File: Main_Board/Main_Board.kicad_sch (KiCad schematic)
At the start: 3 parts, among them U1 TCR2EF33_LMCT

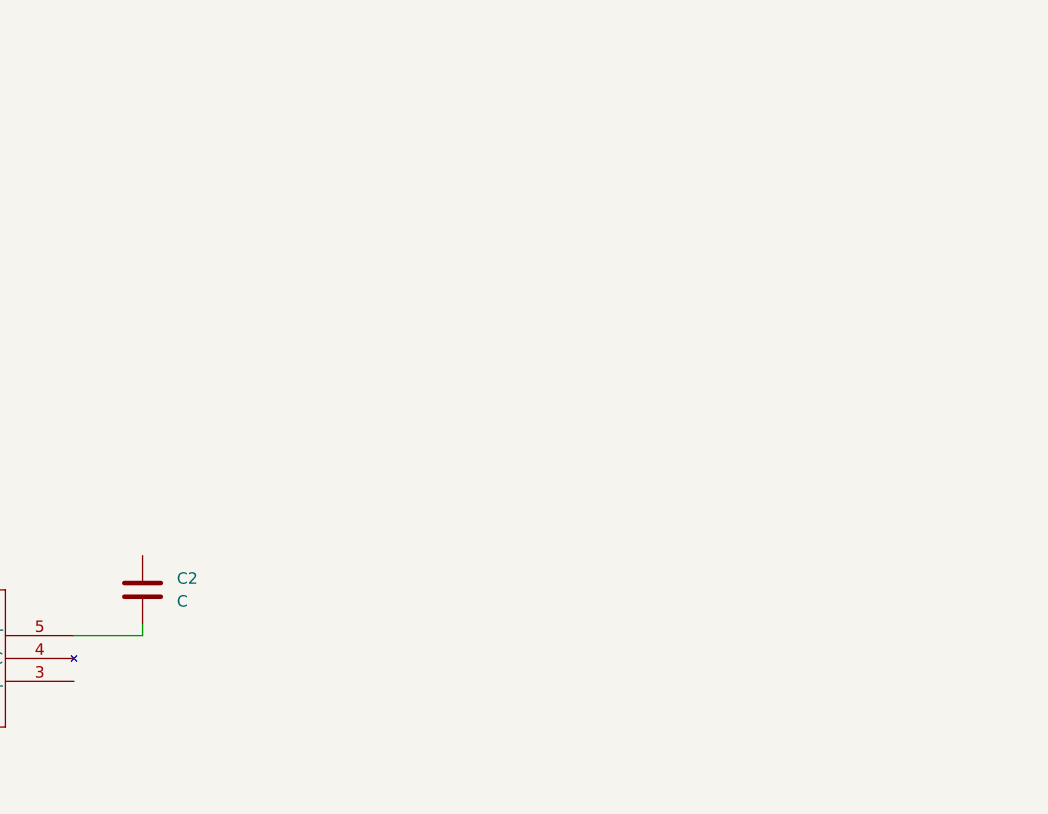
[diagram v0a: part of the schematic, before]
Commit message: Full power input
clean power supply, though it hasn't been updated to connect with the esp
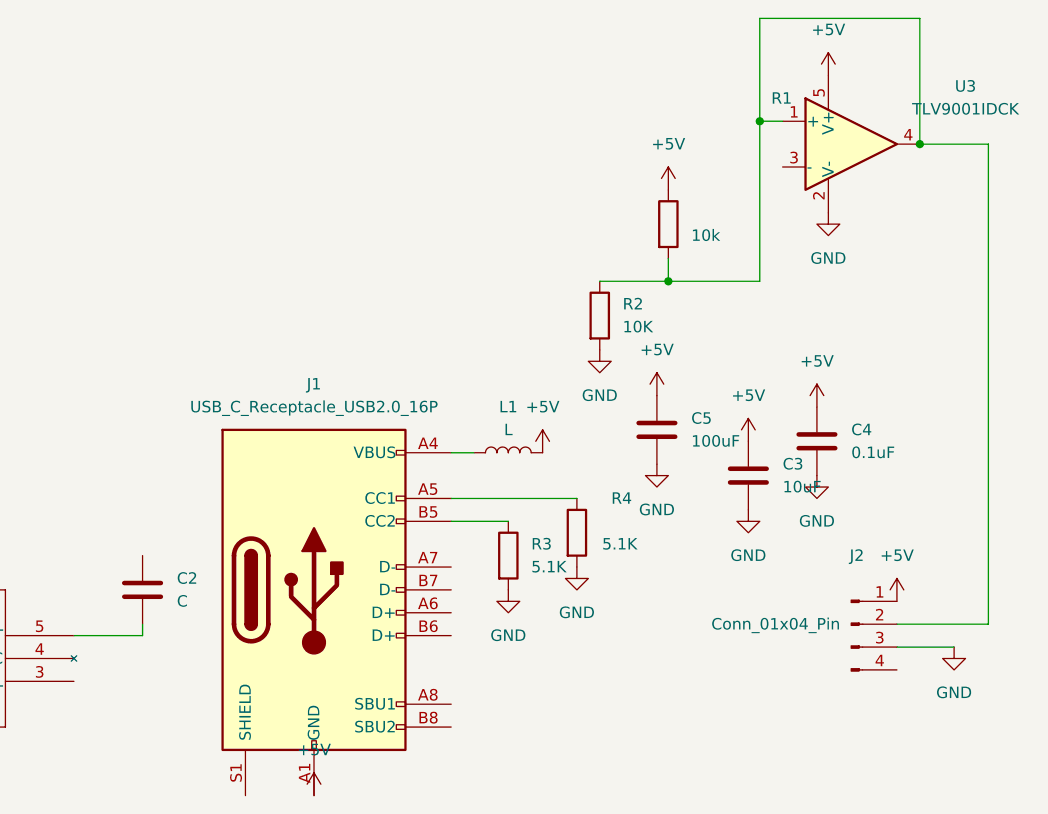
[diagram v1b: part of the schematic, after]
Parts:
- added C3: 10uF, symbol Device:C
- added C4: 0.1uF, symbol Device:C
- added C5: 100uF, symbol Device:C
- added J1: USB_C_Receptacle_USB2.0_16P, symbol Connector:USB_C_Receptacle_USB2.0_16P
- added J2: Conn_01x04_Pin, symbol Connector:Conn_01x04_Pin
- added L1: L, symbol Device:L
- added R1: 10k, symbol Device:R
- added R2: 10K, symbol Device:R
- added R3, R4: 5.1K, symbol Device:R
- added U3: TLV9001IDCK, Package_TO_SOT_SMD:SOT-353_SC-70-5, symbol Amplifier_Operational:TLV9001IDCK
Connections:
- new net: J1.B5 (CC2), R3.1
- new net: J2.2 (Pin_2), R1.2, R2.1, U3.1 (+), U3.4
- new net: J1.A4 (VBUS), J1.A9 (VBUS), J1.B4 (VBUS), J1.B9 (VBUS), L1.1
- new net: J1.A5 (CC1), R4.1
- new net +5V: C3.1, C4.1, C5.1, J1.A1 (GND), J1.A12 (GND), J1.B1 (GND), J1.B12 (GND), J2.1 (Pin_1), L1.2, R1.1, U3.5 (V+)
- new net GND: C3.2, C4.2, C5.2, J2.3 (Pin_3), R2.2, R3.2, R4.2, U3.2 (V-)
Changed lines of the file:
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@@
 (kicad_sch
-	(version 20231120)
+	(version 20250114)
 	(generator "eeschema")
-	(generator_version "8.0")
+	(generator_version "9.0")
 	(paper "A4")

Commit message: Main board
The schematic is done, tho I have some concerns...
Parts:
- removed C1, C2: C, Capacitor_SMD:C_1206_3216Metric_Pad1.33x1.80mm_HandSolder, symbol Device:C
- removed U1: TCR2EF33_LMCT, shared_footprints:SOT-25 SMV_TOS, symbol shared_symbols:TCR2EF33_LMCT
- added J3: Conn_01x05_Pin, Connector_PinHeader_2.54mm:PinHeader_1x01_P2.54mm_Vertical, symbol Connector:Conn_01x05_Pin
- added J4: Conn_01x03_Pin, Connector_PinHeader_2.54mm:PinHeader_1x01_P2.54mm_Vertical, symbol Connector:Conn_01x03_Pin
- added R5, R6: 4.7K, Resistor_SMD:R_0805_2012Metric_Pad1.20x1.40mm_HandSolder, symbol Device:R
- added U1: DEV-15583, Connector_PinHeader_2.54mm:PinHeader_2x14_P2.54mm_Vertical, symbol shared_symbols:DEV-15583
- added U2: ESP32-WROOM-32, RF_Module:ESP32-WROOM-32, symbol RF_Module:ESP32-WROOM-32
- C3, C4, C5: footprint (none) -> Capacitor_SMD:C_0805_2012Metric_Pad1.18x1.45mm_HandSolder
- J1: footprint (none) -> Connector_USB:USB_C_Receptacle_HRO_TYPE-C-31-M-17
- J2: footprint (none) -> Connector_PinHeader_2.54mm:PinHeader_1x01_P2.54mm_Vertical
- L1: footprint (none) -> Inductor_SMD:L_0805_2012Metric
- R1, R2, R3, R4: footprint (none) -> Resistor_SMD:R_0805_2012Metric_Pad1.20x1.40mm_HandSolder
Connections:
- net +5V: now also U1.VIN
- net GND: now also U1.G3, U2.1 (GND), U2.15 (GND), U2.38 (GND), U2.39 (GND)
- new net: J3.5 (Pin_5), U1.10
- new net: J3.2 (Pin_2), U1.11
- new net: J3.3 (Pin_3), U1.12
- new net: J3.1 (Pin_1), U1.13
- new net: J4.1 (Pin_1), U1.14
- new net: J4.2 (Pin_2), U1.15
- new net: R5.2, U1.16, U2.36 (IO22)
- new net: R6.2, U1.17, U2.33 (IO21)
- new net: U1.18, U2.21 (SDO/SD0)
- new net: U1.19, U2.5 (SENSOR_VN)
- new net: U1.20, U2.4 (SENSOR_VP)
- new net: U1.21, U2.3 (EN)
- new net: J4.3 (Pin_3), U1.22
- new net: J3.4 (Pin_4), U1.9
- new net +3.3V: R5.1, R6.1
- no-connect marks 0 -> 54
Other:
- moved on the sheet: C3, C4, C5, J1, J2, L1, R1, R2, R3, R4, U3

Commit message: updated main PCB
same thing
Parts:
- removed U2: ESP32-WROOM-32, RF_Module:ESP32-WROOM-32, symbol RF_Module:ESP32-WROOM-32
- added U2: XIAO-ESP32-C3-DIP, RF_Module:MCU_Seeed_ESP32C3, symbol Seeed_Studio_XIAO_Series:XIAO-ESP32-C3-DIP
- J1: footprint Connector_USB:USB_C_Receptacle_HRO_TYPE-C-31-M-17 -> Connector_USB:USB_C_Receptacle_HRO_TYPE-C-31-M-12
- J2: footprint Connector_PinHeader_2.54mm:PinHeader_1x01_P2.54mm_Vertical -> Connector_PinHeader_2.54mm:PinHeader_1x04_P2.54mm_Vertical
- J3: footprint Connector_PinHeader_2.54mm:PinHeader_1x01_P2.54mm_Vertical -> Connector_PinHeader_2.54mm:PinHeader_1x05_P2.54mm_Vertical
- J4: footprint Connector_PinHeader_2.54mm:PinHeader_1x01_P2.54mm_Vertical -> Connector_PinHeader_2.54mm:PinHeader_1x03_P2.54mm_Vertical
- U1: footprint Connector_PinHeader_2.54mm:PinHeader_2x14_P2.54mm_Vertical -> shared_footprints:MODULE_DEV-15583
- U3: footprint Package_TO_SOT_SMD:SOT-353_SC-70-5 -> Package_TO_SOT_THT:TO-92_Inline
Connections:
- net +5V: now also U2.14 (VBUS)
- net GND: now also U2.13 (GND)
- net at R5.2, U1.16: now also U2.6 (GPIO7/D5/SCL)
- net at R6.2, U1.17: now also U2.5 (GPIO6/D4/SDA)
- net at U1.19: now also U2.2 (GPIO3/A1/D1)
- net at U1.20: now also U2.1 (GPIO2/A0/D0)
- net at U1.21: now also U2.4 (GPIO5/A3/D3)
- no-connect marks 54 -> 34

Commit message: organized
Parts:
- removed J2: Conn_01x04_Pin, Connector_PinHeader_2.54mm:PinHeader_1x04_P2.54mm_Vertical, symbol Connector:Conn_01x04_Pin
- removed L1: L, Inductor_SMD:L_0805_2012Metric, symbol Device:L
- added J5: Conn_01x03_Pin, Connector_PinHeader_2.54mm:PinHeader_1x03_P2.54mm_Vertical, symbol Connector:Conn_01x03_Pin
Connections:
- net +3.3V: now also R6.2, U1.3.3V_2; no longer R6.1
- net +5V: now also J1.A4 (VBUS), J1.A9 (VBUS), J1.B4 (VBUS), J1.B9 (VBUS), J5.1 (Pin_1); no longer J1.A1 (GND), J1.A12 (GND), J1.B1 (GND), J1.B12 (GND)
- net GND: now also J1.A1 (GND), J1.A12 (GND), J1.B1 (GND), J1.B12 (GND), J1.S1 (SHIELD), J5.3 (Pin_3)
- net SCl: now reaches R5.2, U2.6 (GPIO7/D5/SCL)
- net SCl: no longer U1.16
- net SDA: now reaches U1.17, U2.5 (GPIO6/D4/SDA)
- net SDA: now also R6.1; no longer R6.2
- net GPI03: now reaches U1.19, U2.2 (GPIO3/A1/D1)
- net GPI02: now reaches U1.20
- net GPI02: no longer U2.1 (GPIO2/A0/D0)
- net GPIO5: now reaches U1.21, U2.4 (GPIO5/A3/D3)
- new net 2.5V: J5.2 (Pin_2)
- new net GPIO2: U2.1 (GPIO2/A0/D0)
- new net SCL: U1.16
- no-connect marks 34 -> 31
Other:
- moved on the sheet: C3, C4, C5, J1, J3, J4, R1, R2, R3, R4, R5, R6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

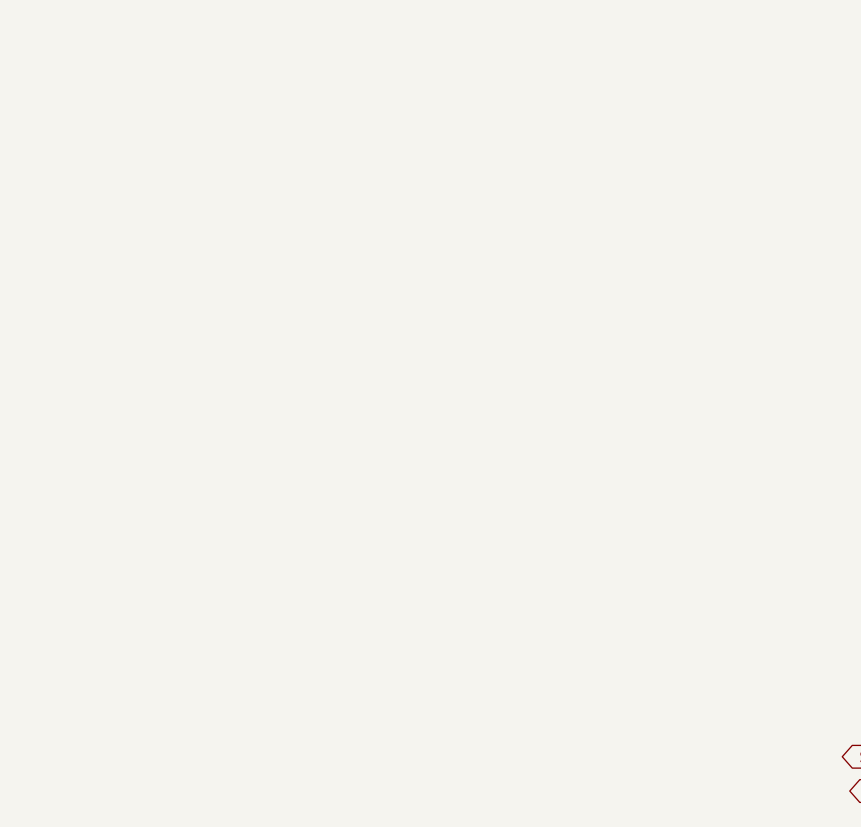
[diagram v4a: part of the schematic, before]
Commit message: added 555 timer
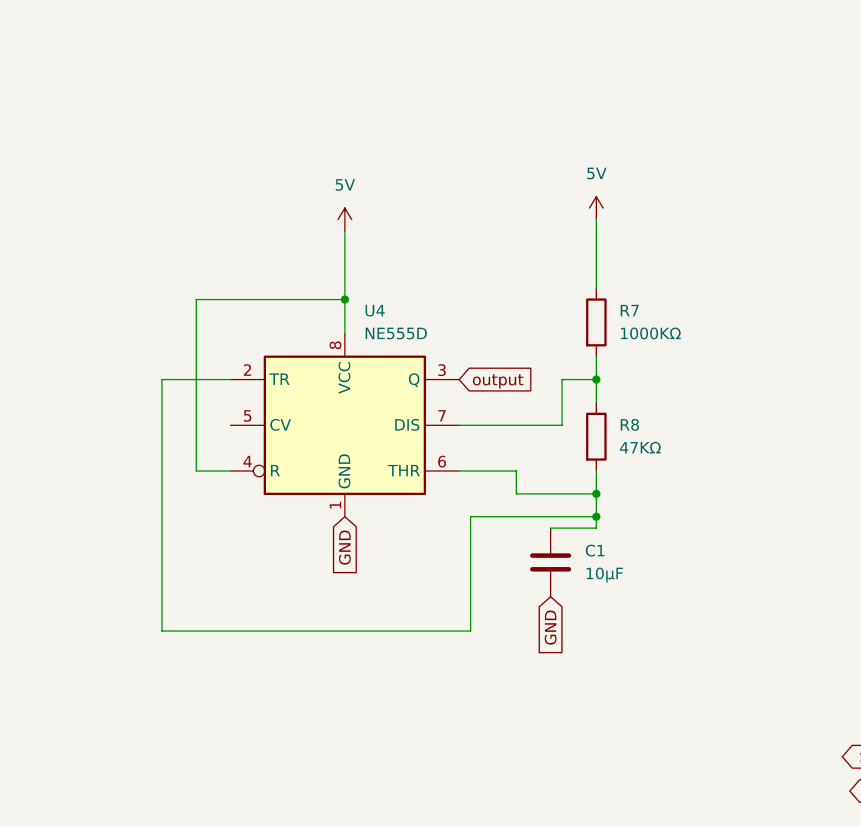
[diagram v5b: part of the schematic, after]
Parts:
- added C1: 10μF, symbol Device:C
- added R7: 1000KΩ, symbol Device:R
- added R8: 47KΩ, symbol Device:R
- added U4: NE555D, Package_SO:SOIC-8_3.9x4.9mm_P1.27mm, symbol Timer:NE555D
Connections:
- net GND: now also C1.2, U4.1 (GND)
- new net: C1.1, R8.2, U4.2 (TR), U4.6 (THR)
- new net: R7.2, R8.1, U4.7 (DIS)
- new net 5V: R7.1, U4.4 (R), U4.8 (VCC)
- new net output: U4.3 (Q)

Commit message: jst sh
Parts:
- C1: footprint (none) -> Capacitor_SMD:C_0805_2012Metric_Pad1.18x1.45mm_HandSolder
- J3: footprint Connector_PinHeader_2.54mm:PinHeader_1x05_P2.54mm_Vertical -> Connector_JST:JST_SH_SM05B-SRSS-TB_1x05-1MP_P1.00mm_Horizontal
- J4: footprint Connector_PinHeader_2.54mm:PinHeader_1x03_P2.54mm_Vertical -> Connector_JST:JST_SH_SM03B-SRSS-TB_1x03-1MP_P1.00mm_Horizontal
- J5: footprint Connector_PinHeader_2.54mm:PinHeader_1x03_P2.54mm_Vertical -> Connector_JST:JST_SH_SM02B-SRSS-TB_1x02-1MP_P1.00mm_Horizontal
- R7, R8: footprint (none) -> Resistor_SMD:R_0805_2012Metric_Pad1.20x1.40mm_HandSolder
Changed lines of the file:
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@@
 			)
 		)
-		(property "Footprint" ""
+		(property "Footprint" "Capacitor_SMD:C_0805_2012Metric_Pad1.18x1.45mm_HandSolder"
 			(at 117.8052 123.19 0)
 			(effects
@@
 			)
 		)
-		(property "Footprint" "Connector_PinHeader_2.54mm:PinHeader_1x03_P2.54mm_Vertical"
+		(property "Footprint" "Connector_JST:JST_SH_SM02B-SRSS-TB_1x02-1MP_P1.00mm_Horizontal"
 			(at 254 156.21 0)
 			(effects
@@
 			)
 		)
-		(property "Footprint" ""
+		(property "Footprint" "Resistor_SMD:R_0805_2012Metric_Pad1.20x1.40mm_HandSolder"
 			(at 120.142 92.71 90)
 			(effects
@@
 			)
 		)
-		(property "Footprint" ""
+		(property "Footprint" "Resistor_SMD:R_0805_2012Metric_Pad1.20x1.40mm_HandSolder"
 			(at 120.142 105.41 90)
 			(effects
@@
 			)
 		)
-		(property "Footprint" "Connector_PinHeader_2.54mm:PinHeader_1x03_P2.54mm_Vertical"
+		(property "Footprint" "Connector_JST:JST_SH_SM03B-SRSS-TB_1x03-1MP_P1.00mm_Horizontal"
 			(at 262.89 58.42 0)
 			(effects
@@
 			)
 		)
-		(property "Footprint" "Connector_PinHeader_2.54mm:PinHeader_1x05_P2.54mm_Vertical"
+		(property "Footprint" "Connector_JST:JST_SH_SM05B-SRSS-TB_1x05-1MP_P1.00mm_Horizontal"
 			(at 189.23 45.72 0)
 			(effects

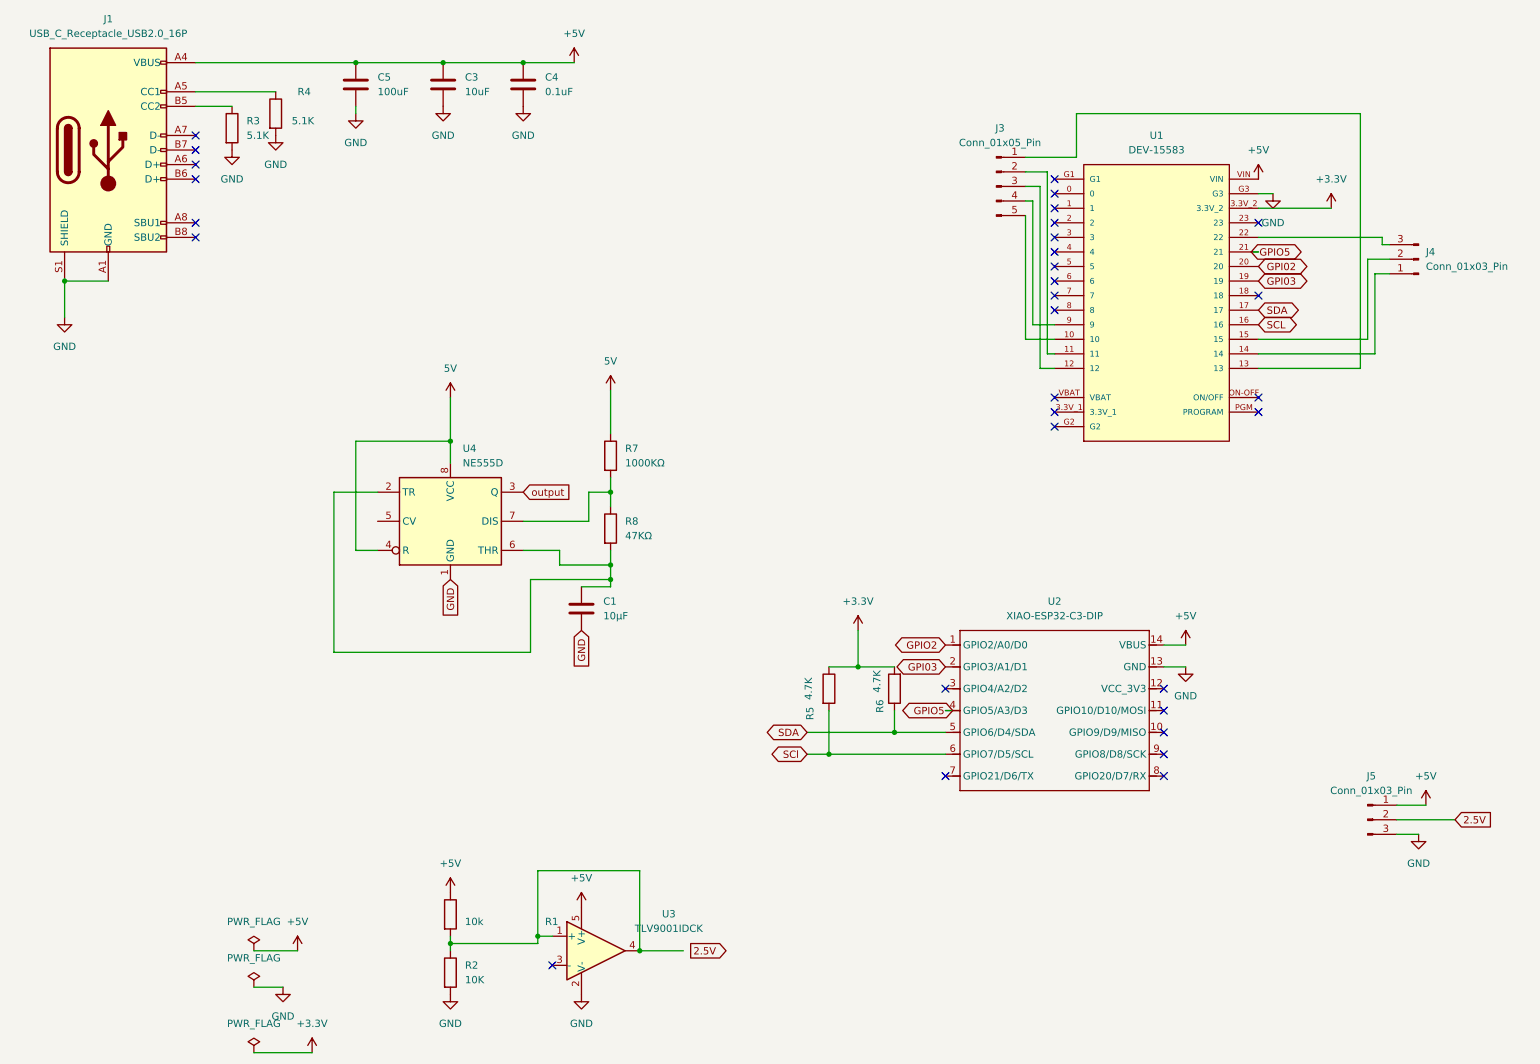
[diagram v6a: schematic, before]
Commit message: replaced opamp with LDO, completed layout
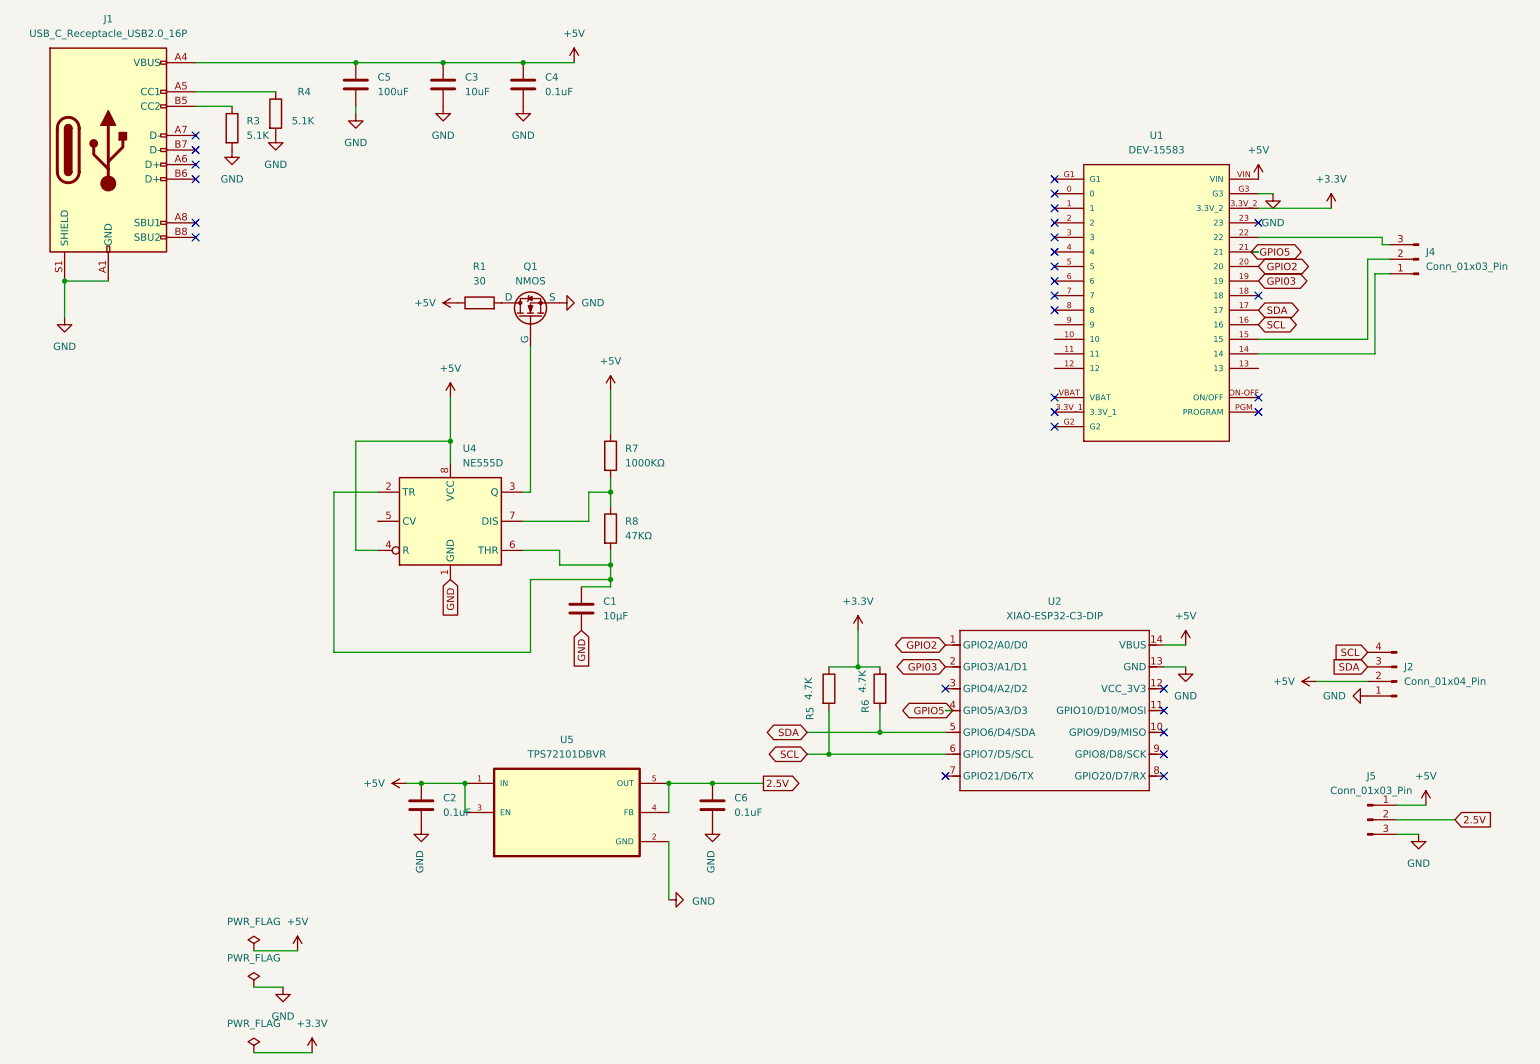
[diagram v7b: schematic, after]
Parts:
- removed J3: Conn_01x05_Pin, Connector_JST:JST_SH_SM05B-SRSS-TB_1x05-1MP_P1.00mm_Horizontal, symbol Connector:Conn_01x05_Pin
- removed R2: 10K, Resistor_SMD:R_0805_2012Metric_Pad1.20x1.40mm_HandSolder, symbol Device:R
- removed U3: TLV9001IDCK, Package_TO_SOT_THT:TO-92_Inline, symbol Amplifier_Operational:TLV9001IDCK
- added C2, C6: 0.1uF, Capacitor_SMD:C_0805_2012Metric_Pad1.18x1.45mm_HandSolder, symbol Device:C
- added J2: Conn_01x04_Pin, Connector_JST:JST_SH_SM04B-SRSS-TB_1x04-1MP_P1.00mm_Horizontal, symbol Connector:Conn_01x04_Pin
- added Q1: NMOS, Package_TO_SOT_SMD:SOT-323_SC-70, symbol Simulation_SPICE:NMOS
- added U5: TPS72101DBVR, Package_TO_SOT_SMD:SOT-23-5_HandSoldering, symbol shared_symbols:TPS72101DBVR
- J5: footprint Connector_JST:JST_SH_SM02B-SRSS-TB_1x02-1MP_P1.00mm_Horizontal -> Connector_JST:JST_SH_SM03B-SRSS-TB_1x03-1MP_P1.00mm_Horizontal
- R1: value 10k -> 30
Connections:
- net 5V is gone; now on net +5V: R7.1, U4.4 (R), U4.8 (VCC)
- net GPI02 is gone; now on net GPIO2: U1.20
- net SCl is gone; now on net SCL: R5.2, U2.6 (GPIO7/D5/SCL)
- net +5V: now also C2.1, J2.2 (Pin_2), U5.1 (IN), U5.3 (EN)
- net 2.5V: now also C6.1, U5.4 (FB), U5.5 (OUT)
- net GND: now also C2.2, C6.2, J2.1 (Pin_1), Q1.3 (S), U5.2 (GND)
- net SCL: now also J2.4 (Pin_4)
- net SDA: now also J2.3 (Pin_3)
- net at R1.2: now also Q1.1 (D)
- net output: no longer names the net of U4.3 (Q)
- net output: now also Q1.2 (G)
- no-connect marks 31 -> 30
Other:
- moved on the sheet: R6
